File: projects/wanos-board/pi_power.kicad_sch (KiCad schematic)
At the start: 8 parts, among them J17 5V_IN, J40 Raspberry_Pi_4

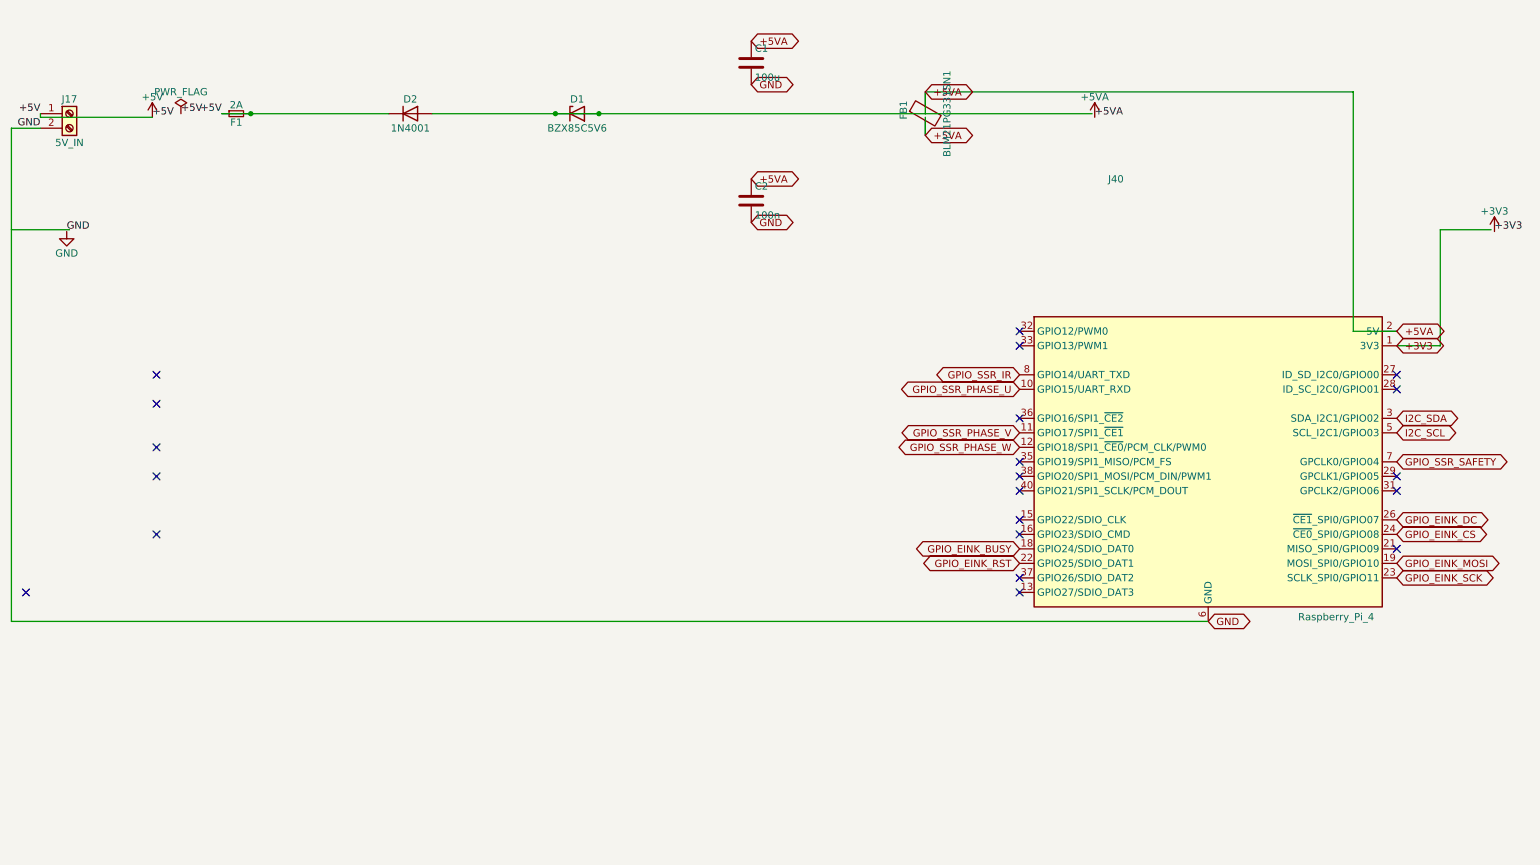
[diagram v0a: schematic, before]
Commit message: pi_power & 12V_monitor schematics OK added datasheets doc update
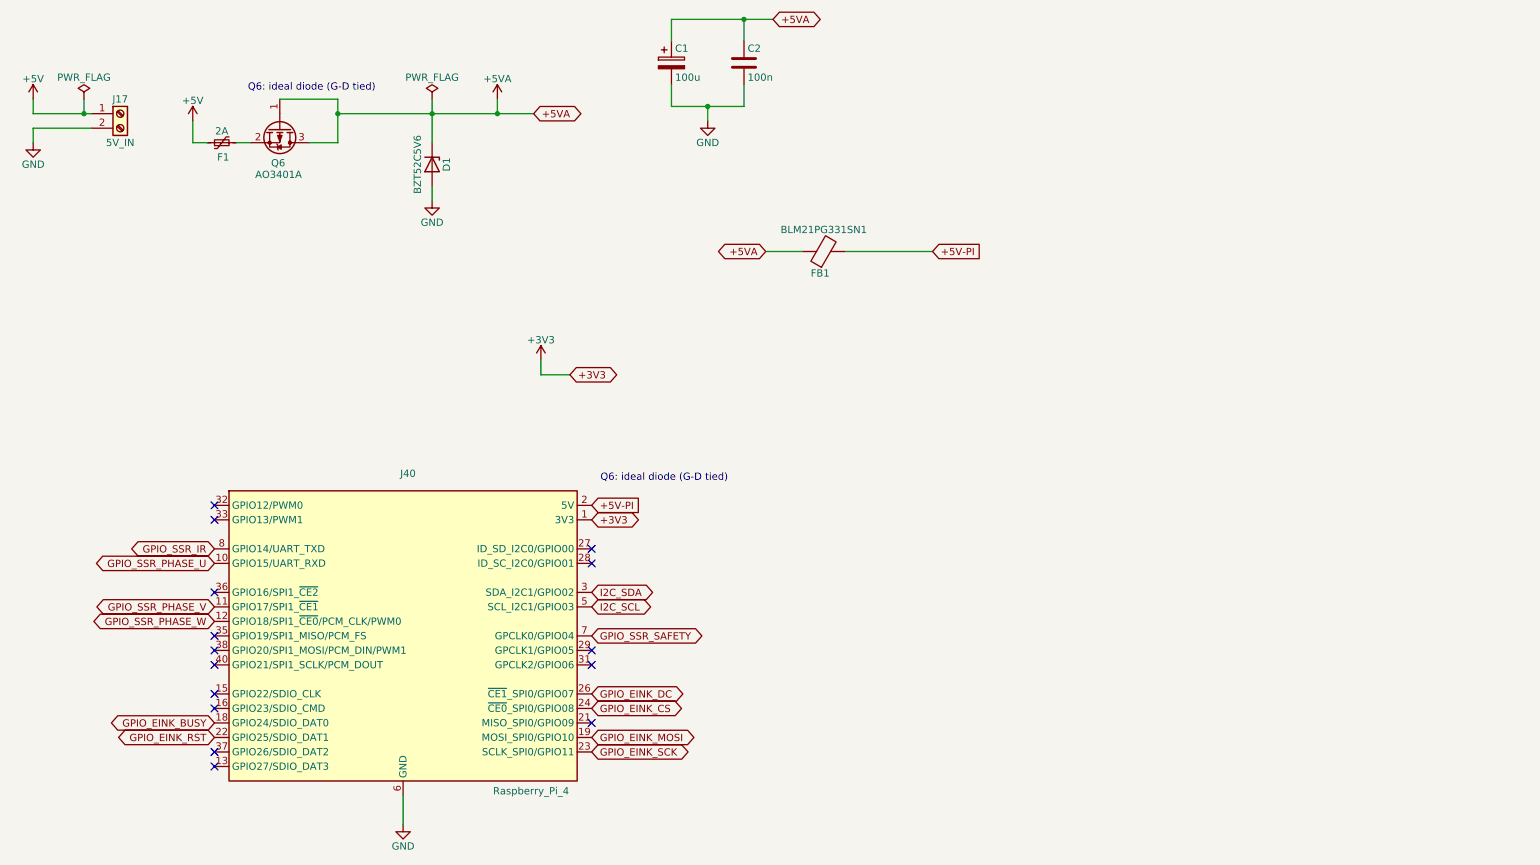
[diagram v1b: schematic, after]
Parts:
- removed D2: 1N4001, Diode_THT:D_DO-41_SOD81_P7.62mm_Horizontal, symbol Diode:1N4002
- added Q6: AO3401A, Package_TO_SOT_SMD:SOT-23, symbol Transistor_FET:AO3401A
- C1: footprint Capacitor_THT:CP_Radial_D10.0mm_P5.00mm -> Capacitor_SMD:CP_Elec_6.3x5.4mm; symbol Device:C -> Device:C_Polarized
- D1: value BZX85C5V6 -> BZT52C5V6; footprint Diode_THT:D_DO-41_SOD81_P7.62mm_Horizontal -> Diode_SMD:D_SOD-123
- F1: footprint Fuse:Fuseholder_Cylinder-5x20mm_Schurter_0031_8201_Horizontal_Open -> Fuse:Fuse_1206_3216Metric; symbol Device:Fuse_Small -> Device:Polyfuse_Small
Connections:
- net +5V: no longer F1.2
- net +5VA: now also Q6.1 (G), Q6.3 (D); no longer D1.2 (A), FB1.2, J40.2 (5V), J40.4 (5V)
- net GND: now also D1.2 (A)
- new net: F1.2, Q6.2 (S)
- new net +5V-PI: FB1.2, J40.2 (5V), J40.4 (5V)
- no-connect marks 21 -> 15
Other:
- note added: "Q6: ideal diode (G-D tied)"
- moved on the sheet: C2, D1, FB1, J17, J40

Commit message: SSR, power, IO_expander schemas update
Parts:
- added C17: 100n, Capacitor_SMD:C_0805_2012Metric, symbol Device:C
- added D23, D24: LED, LED_SMD:LED_0805_2012Metric, symbol Device:LED
- added D3: SMBJ12A, Diode_SMD:D_SMB, symbol Device:D_TVS
- added J14: 12V_IN, TerminalBlock_Phoenix:TerminalBlock_Phoenix_MKDS-1,5-2-5.08_1x02_P5.08mm_Horizontal, symbol Connector:Screw_Terminal_01x02
- added R29: 2k, Resistor_SMD:R_0805_2012Metric, symbol Device:R
- added R30: 6k8, Resistor_SMD:R_0805_2012Metric, symbol Device:R
- added R32: 1k5, Resistor_SMD:R_0805_2012Metric, symbol Device:R
- added R33: 10k, Resistor_SMD:R_0805_2012Metric, symbol Device:R
- added U4: PC817A, Package_SO:SO-4_4.4x3.9mm_P2.54mm, symbol Isolator:PC817
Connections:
- net +3V3: now also R33.1
- net +5VA: now also R29.1
- net GND: now also C17.2, D23.1 (K), D24.1 (K), D3.2 (A2), J14.2 (Pin_2), U4.2, U4.3
- new net: D23.2 (A), R29.2
- new net: D24.2 (A), R30.2
- new net: R32.1, U4.1
- new net +12V: D3.1 (A1), J14.1 (Pin_1), R30.1, R32.2
- new net EXP_B_P6_12V_MON: C17.1, R33.2, U4.4
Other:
- note added: "pin2 = pin4"
- note added: "pullup"
- moved on the sheet: C1, C2, FB1
